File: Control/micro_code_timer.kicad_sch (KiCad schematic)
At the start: 8 parts, among them U5 74LS163, U6 74HCT138

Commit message: Control routed on PCB
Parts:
- D17, D18, D19: footprint (none) -> LED_THT:LED_D5.0mm
- R17, R18, R19: footprint (none) -> _DownloadFootprints:CF_series_Resistors_THT
- U5, U6: footprint (none) -> Package_DIP:DIP-16_W7.62mm
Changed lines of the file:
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@@
 			)
 		)
-		(property "Footprint" ""
+		(property "Footprint" "Package_DIP:DIP-16_W7.62mm"
 			(at 134.62 59.69 0)
 			(effects
@@
 			)
 		)
-		(property "Footprint" ""
+		(property "Footprint" "_DownloadFootprints:CF_series_Resistors_THT"
 			(at 94.742 69.85 90)
 			(effects
@@
 			)
 		)
-		(property "Footprint" ""
+		(property "Footprint" "_DownloadFootprints:CF_series_Resistors_THT"
 			(at 103.632 69.85 90)
 			(effects
@@
 			)
 		)
-		(property "Footprint" ""
+		(property "Footprint" "LED_THT:LED_D5.0mm"
 			(at 96.52 60.96 0)
 			(effects
@@
 			)
 		)
-		(property "Footprint" ""
+		(property "Footprint" "LED_THT:LED_D5.0mm"
 			(at 105.41 60.96 0)
 			(effects
@@
 			)
 		)
-		(property "Footprint" ""
+		(property "Footprint" "LED_THT:LED_D5.0mm"
 			(at 87.63 60.96 0)
 			(effects
@@
 			)
 		)
-		(property "Footprint" ""
+		(property "Footprint" "_DownloadFootprints:CF_series_Resistors_THT"
 			(at 85.852 69.85 90)
 			(effects
@@
 			)
 		)
-		(property "Footprint" ""
+		(property "Footprint" "Package_DIP:DIP-16_W7.62mm"
 			(at 66.04 62.23 0)
 			(effects

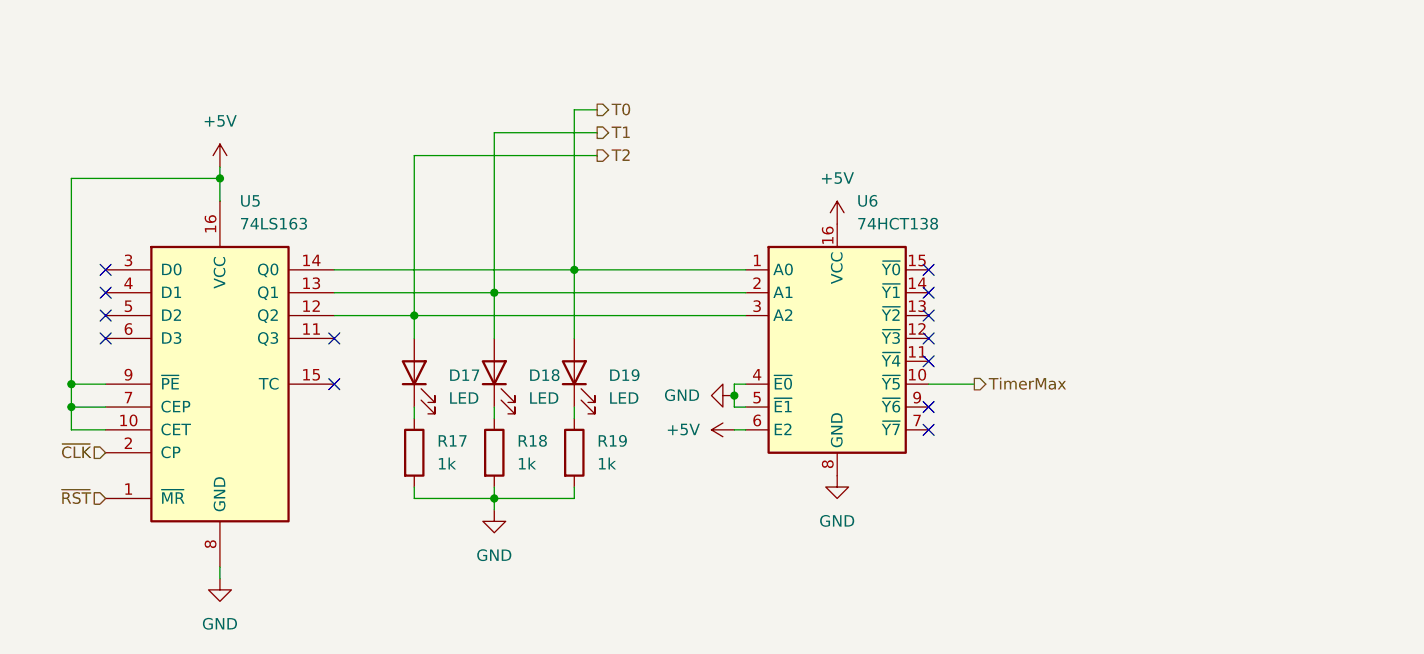
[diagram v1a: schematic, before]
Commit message: Updated microcode timer LEDs to 1 hot signal instead of binary counter
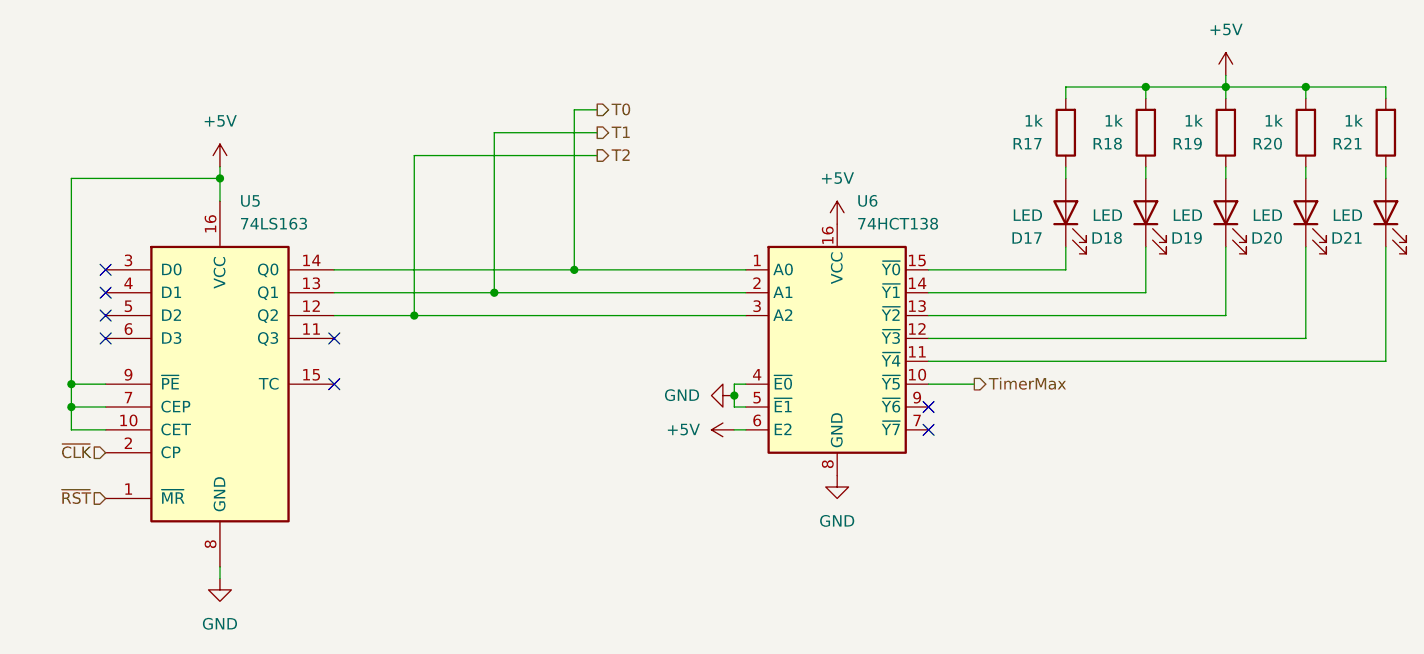
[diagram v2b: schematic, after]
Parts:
- added D20, D21: LED, LED_THT:LED_D5.0mm, symbol Device:LED
- added R20, R21: 1k, _DownloadFootprints:CF_series_Resistors_THT, symbol Device:R
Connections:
- net +5V: now also R17.2, R18.2, R19.2, R20.2, R21.2
- net GND: no longer R17.2, R18.2, R19.2
- net T0: no longer D19.2 (A)
- net T1: no longer D18.2 (A)
- net T2: no longer D17.2 (A)
- net at U6.11 (~{Y4}): now also D21.1 (K)
- net at U6.12 (~{Y3}): now also D20.1 (K)
- net at U6.13 (~{Y2}): now also D19.1 (K)
- net at U6.14 (~{Y1}): now also D18.1 (K)
- net at U6.15 (~{Y0}): now also D17.1 (K)
- net at R18.1: now also D18.2 (A); no longer D18.1 (K)
- net at R19.1: now also D19.2 (A); no longer D19.1 (K)
- net at R17.1: now also D17.2 (A); no longer D17.1 (K)
- new net: D21.2 (A), R21.1
- new net: D20.2 (A), R20.1
- no-connect marks 13 -> 8

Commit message: Added spare pins to control
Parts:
- renumbered R17 to R20, R18 to R21, R19 to R22, R20 to R23, R21 to R24
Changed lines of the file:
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@@
 		(dnp no)
 		(fields_autoplaced yes)
-		(property "Reference" "R17"
+		(property "Reference" "R20"
 			(at 157.48 35.5601 0)
 			(effects
@@
 			(project "Control"
 				(path "/460bc1d8-5a70-4cad-87d6-3febe61be174/b7d20669-2734-4065-865d-52ffdeebffcb"
-					(reference "R17")
+					(reference "R20")
 					(unit 1)
 				)
@@
 		(dnp no)
 		(fields_autoplaced yes)
-		(property "Reference" "#PWR027"
+		(property "Reference" "#PWR024"
 			(at 66.04 90.17 0)
 			(effects
@@
 			(project ""
 				(path "/460bc1d8-5a70-4cad-87d6-3febe61be174/b7d20669-2734-4065-865d-52ffdeebffcb"
-					(reference "#PWR027")
+					(reference "#PWR024")
 					(unit 1)
 				)
@@
 		(dnp no)
 		(fields_autoplaced yes)
-		(property "Reference" "#PWR032"
+		(property "Reference" "#PWR029"
 			(at 177.8 31.75 0)
 			(effects
@@
 			(project "Control"
 				(path "/460bc1d8-5a70-4cad-87d6-3febe61be174/b7d20669-2734-4065-865d-52ffdeebffcb"
-					(reference "#PWR032")
+					(reference "#PWR029")
 					(unit 1)
 				)
@@
 		(dnp no)
 		(fields_autoplaced yes)
-		(property "Reference" "R21"
+		(property "Reference" "R24"
 			(at 193.04 35.5601 0)
 			(effects
@@
 			(project "Control"
 				(path "/460bc1d8-5a70-4cad-87d6-3febe61be174/b7d20669-2734-4065-865d-52ffdeebffcb"
-					(reference "R21")
+					(reference "R24")
 					(unit 1)
 				)
@@
 		(dnp no)
 		(fields_autoplaced yes)
-		(property "Reference" "R18"
+		(property "Reference" "R21"
 			(at 166.37 35.5601 0)
 			(effects
@@
 			(project "Control"
 				(path "/460bc1d8-5a70-4cad-87d6-3febe61be174/b7d20669-2734-4065-865d-52ffdeebffcb"
-					(reference "R18")
+					(reference "R21")
 					(unit 1)
 				)
@@
 		(dnp no)
 		(fields_autoplaced yes)
-		(property "Reference" "R19"
+		(property "Reference" "R22"
 			(at 175.26 35.5601 0)
 			(effects
@@
 			(project "Control"
 				(path "/460bc1d8-5a70-4cad-87d6-3febe61be174/b7d20669-2734-4065-865d-52ffdeebffcb"
-					(reference "R19")
+					(reference "R22")
 					(unit 1)
 				)
@@
 		(dnp no)
 		(fields_autoplaced yes)
-		(property "Reference" "#PWR030"
+		(property "Reference" "#PWR027"
 			(at 134.62 48.26 0)
 			(effects
@@
 			(project "Control"
 				(path "/460bc1d8-5a70-4cad-87d6-3febe61be174/b7d20669-2734-4065-865d-52ffdeebffcb"
-					(reference "#PWR030")
+					(reference "#PWR027")
 					(unit 1)
 				)
@@
 		(dnp no)
 		(fields_autoplaced yes)
-		(property "Reference" "R20"
+		(property "Reference" "R23"
 			(at 184.15 35.5601 0)
 			(effects
@@
 			(project "Control"
 				(path "/460bc1d8-5a70-4cad-87d6-3febe61be174/b7d20669-2734-4065-865d-52ffdeebffcb"
-					(reference "R20")
+					(reference "R23")
 					(unit 1)
 				)
@@
 		(dnp no)
 		(fields_autoplaced yes)
-		(property "Reference" "#PWR031"
+		(property "Reference" "#PWR028"
 			(at 134.62 78.74 0)
 			(effects
@@
 			(project "Control"
 				(path "/460bc1d8-5a70-4cad-87d6-3febe61be174/b7d20669-2734-4065-865d-52ffdeebffcb"
-					(reference "#PWR031")
+					(reference "#PWR028")
 					(unit 1)
 				)
@@
 		(dnp no)
 		(fields_autoplaced yes)
-		(property "Reference" "#PWR029"
+		(property "Reference" "#PWR026"
 			(at 127 67.31 0)
 			(effects
@@
 			(project "Control"
 				(path "/460bc1d8-5a70-4cad-87d6-3febe61be174/b7d20669-2734-4065-865d-52ffdeebffcb"
-					(reference "#PWR029")
+					(reference "#PWR026")
 					(unit 1)
 				)
@@
 		(dnp no)
 		(fields_autoplaced yes)
-		(property "Reference" "#PWR026"
+		(property "Reference" "#PWR023"
 			(at 66.04 41.91 0)
 			(effects
@@
 			(project ""
 				(path "/460bc1d8-5a70-4cad-87d6-3febe61be174/b7d20669-2734-4065-865d-52ffdeebffcb"
-					(reference "#PWR026")
+					(reference "#PWR023")
 					(unit 1)
 				)
@@
 		(dnp no)
 		(fields_autoplaced yes)
-		(property "Reference" "#PWR028"
+		(property "Reference" "#PWR025"
 			(at 116.84 63.5 0)
 			(effects
@@
 			(project "Control"
 				(path "/460bc1d8-5a70-4cad-87d6-3febe61be174/b7d20669-2734-4065-865d-52ffdeebffcb"
-					(reference "#PWR028")
-					(unit 1)
-				)
+					(reference "#PWR025")
+					(unit 1)
+				)
